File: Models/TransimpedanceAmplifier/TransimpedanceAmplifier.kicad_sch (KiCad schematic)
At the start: 9 parts, among them U1 LM78L15ACMX, U2 LM79L15ACMX, U3 LM78L05ACMX, U4 LM79L05ACMX, U5 LM78L05ACMX, U6 LM79L05ACMX

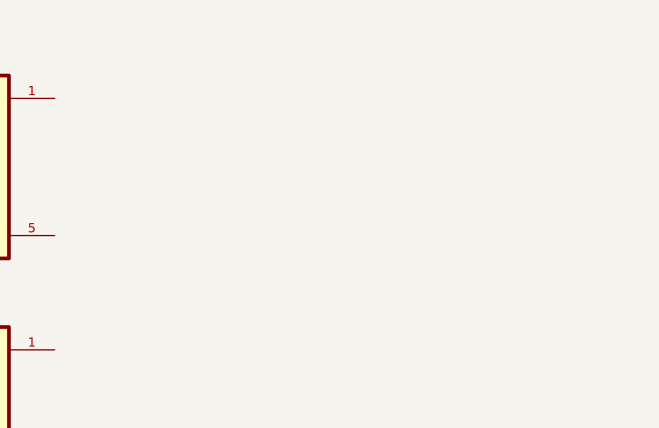
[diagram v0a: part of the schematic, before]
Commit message: Added KiCad libraries for more chips
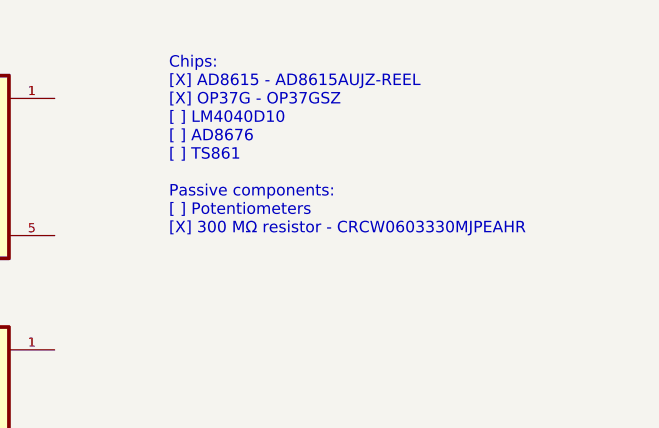
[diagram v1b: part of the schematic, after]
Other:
- note added: "Chips: [X] AD8615 - AD8615AUJZ-REEL [X] OP37G - OP37GSZ [ ] LM4040D10 [ ] AD8676 [ ] TS861 Passive components: [ ] Potentiometers [X] 300 MΩ resistor - CRCW0603330MJPEAHR"
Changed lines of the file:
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@@
 	(generator_version "9.0")
 	(paper "A4")
+	(text "Chips:\n[X] AD8615 - AD8615AUJZ-REEL\n[X] OP37G - OP37GSZ\n[ ] LM4040D10\n[ ] AD8676\n[ ] TS861\n\nPassive components:\n[ ] Potentiometers\n[X] 300 MΩ resistor - CRCW0603330MJPEAHR"
+		(exclude_from_sim no)
+		(at 149.86 38.354 0)
+		(effects
+			(font
+				(size 1.27 1.27)
+			)
+			(justify left)
+		)
+	)
 	(symbol
 		(lib_id "LM78L15ACMX_NOPB:LM78L15ACMX_NOPB")

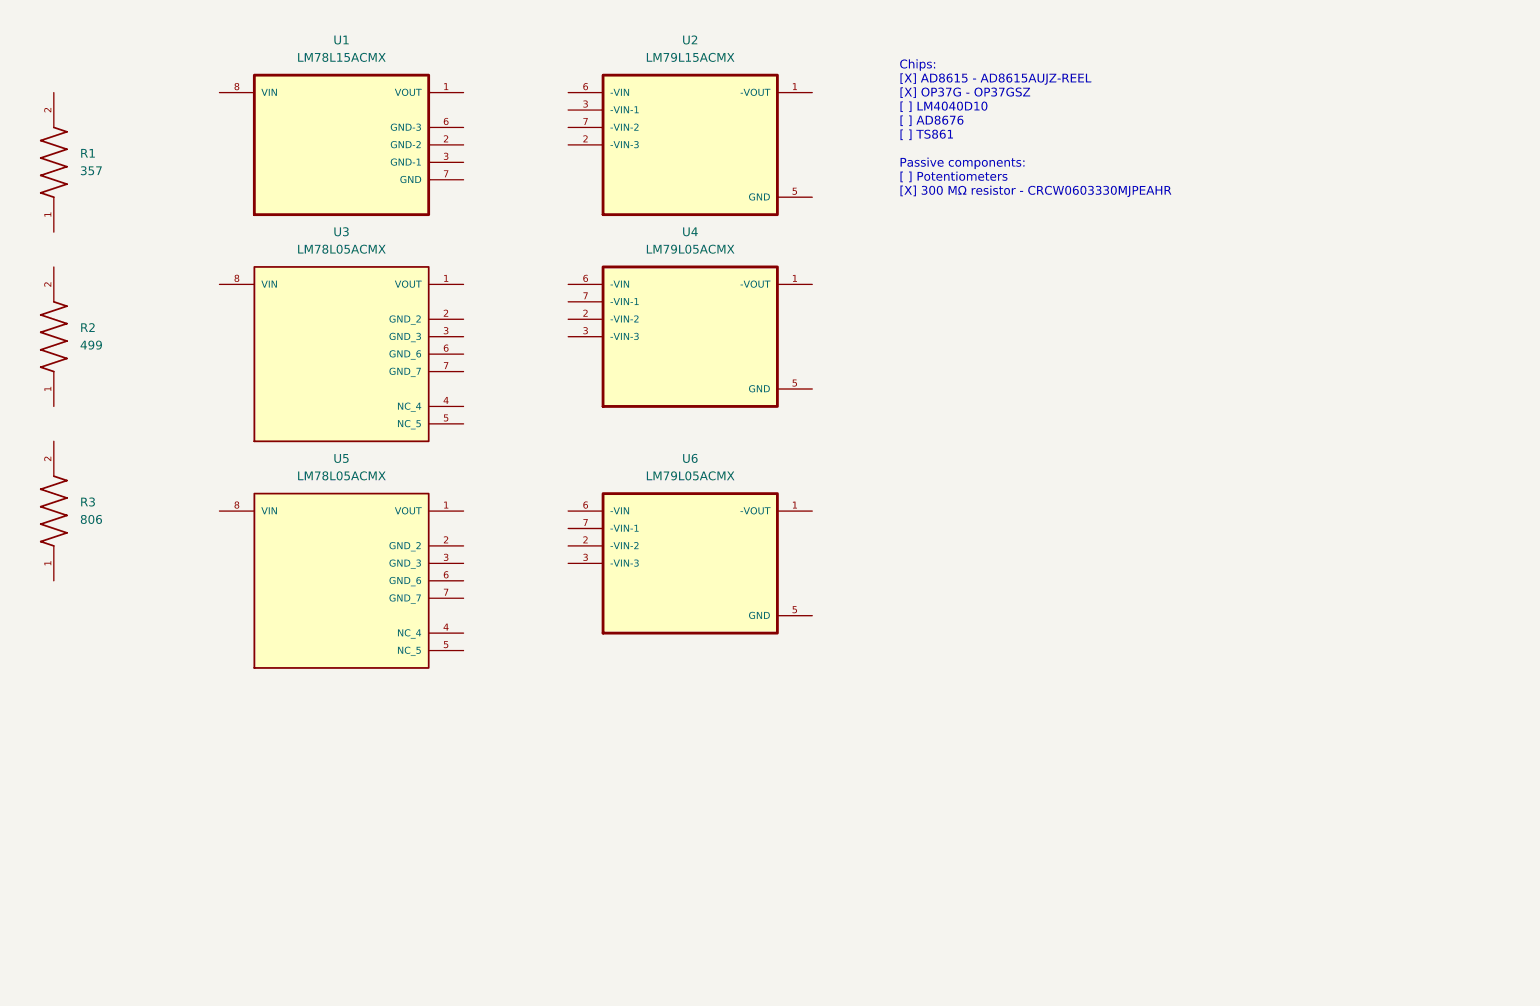
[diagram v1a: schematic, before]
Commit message: Massive cleanup to the libraries for the transimpedance amplifier
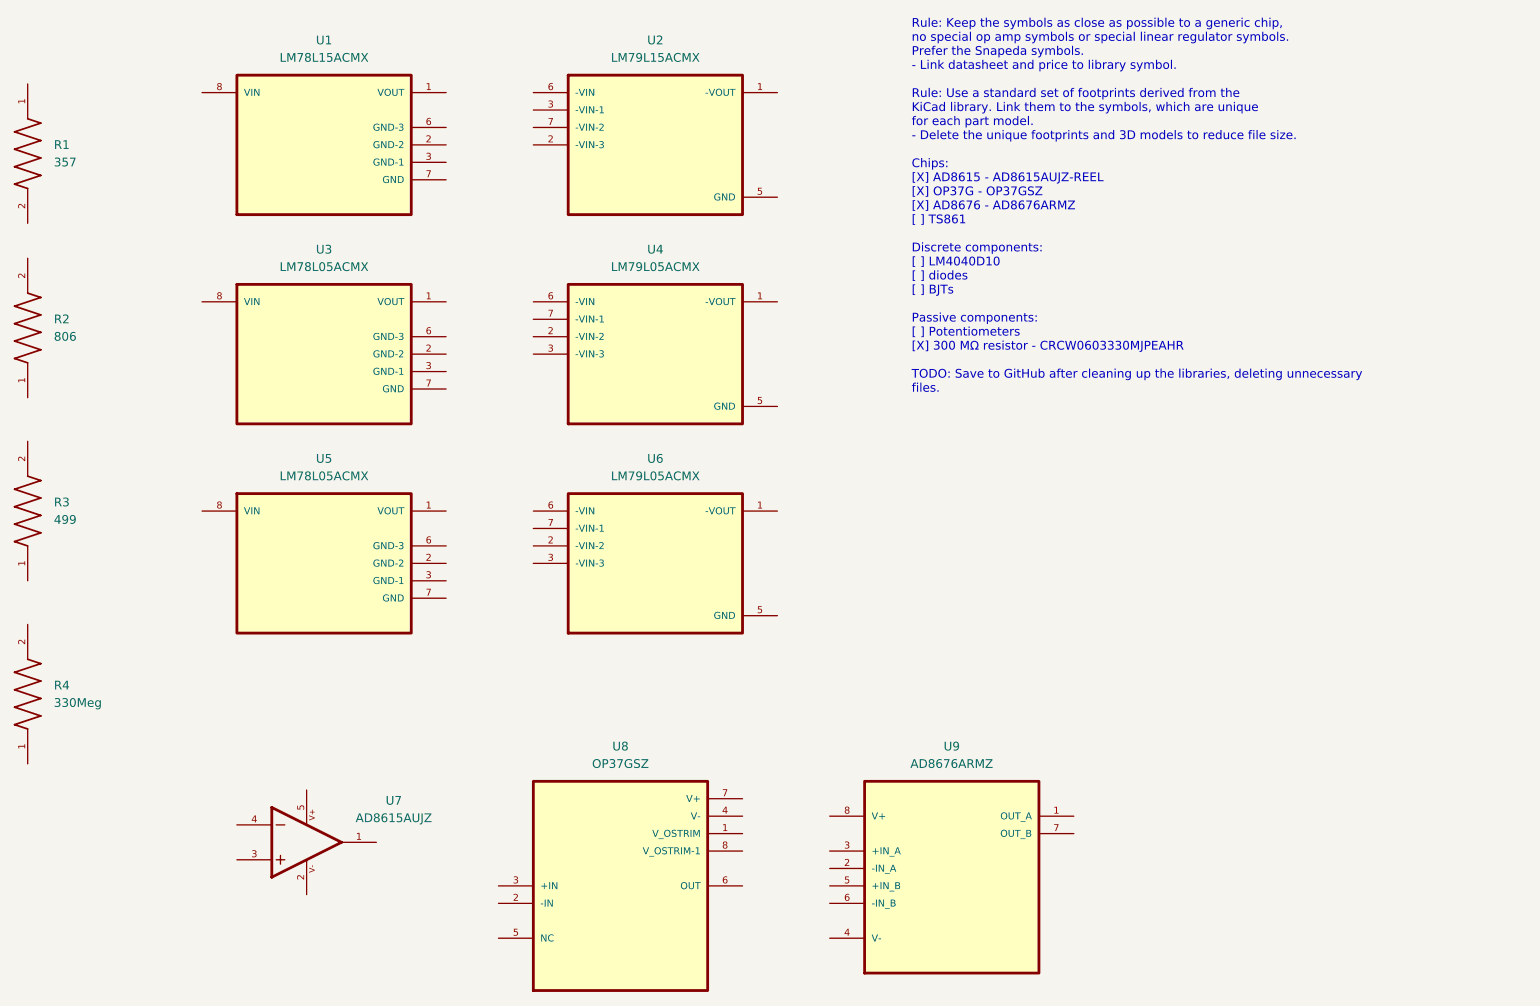
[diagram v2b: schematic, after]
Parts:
- removed R2: 499, CRCW0603499RFKEA:RESC1508X50N, symbol CRCW0603499RFKEA:CRCW0603499RFKEA
- removed R3: 806, CRCW0603806RFKEA:RESC1508X50N, symbol CRCW0603806RFKEA:CRCW0603806RFKEA
- removed U2: LM79L15ACMX, LM79L15ACMX_NOPB_NOPB:SOIC127P599X175-8N, symbol LM79L15ACMX_NOPB_NOPB:LM79L15ACMX_NOPB_NOPB
- added R2: 806, Generic_SMD_Fixed:R_0603_Fixed, symbol CRCW0603806RFKEA:CRCW0603806RFKEA
- added R3: 499, Generic_SMD_Fixed:R_0603_Fixed, symbol CRCW0603499RFKEA:CRCW0603499RFKEA
- added R4: 330Meg, Generic_SMD_Fixed:R_0603_Fixed, symbol CRCW0603330MJPEAHR:CRCW0603330MJPEAHR
- added U2: LM79L15ACMX, Package_SO:SOIC-8_3.9x4.9mm_P1.27mm, symbol LM79L15ACMX_NOPB:LM79L15ACMX_NOPB
- added U7: AD8615AUJZ, Package_TO_SOT_SMD:TSOT-23-5, symbol AD8615AUJZ-REEL:AD8615AUJZ-REEL
- added U8: OP37GSZ, Package_SO:SOIC-8_3.9x4.9mm_P1.27mm, symbol OP37GSZ:OP37GSZ
- added U9: AD8676ARMZ, Package_SO:MSOP-8_3x3mm_P0.65mm, symbol AD8676ARMZ:AD8676ARMZ
- R1: footprint CRCW0603357RFKEA:RESC1508X50N -> Generic_SMD_Fixed:R_0603_Fixed; Availability In Stock -> (none); Check_prices https://www.snapeda.com/parts/CRCW0603357RFKEA/Vishay/view-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 -> (none); Description_1 Resistor;Thick Film;357 Ohms;0.1 W;1%;SMT;0603;TCR 37 ppm/D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 -> (none); MF Vishay -> (none); MP CRCW0603357RFKEA -> (none); Package 1508 Vishay -> (none); SnapEDA_Link https://www.snapeda.com/parts/CRCW0603357RFKEA/Vishay/view-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 -> (none)
- U1: footprint LM78L15ACMX_NOPB:SOIC127P599X175-8N -> Package_SO:SOIC-8_3.9x4.9mm_P1.27mm; Availability In Stock -> (none); Check_prices https://www.snapeda.com/parts/LM78L15ACMX/NOPB/Texas+Instru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 -> (none); Description_1 100-mA, 30-V, linear voltage regulator -> (none); MF Texas Instruments -> (none); MP LM78L15ACMX/NOPB -> (none); Package SOIC-8 Texas Instruments -> (none); SnapEDA_Link https://www.snapeda.com/parts/LM78L15ACMX/NOPB/Texas+Instru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 -> (none)
- U3, U5: footprint LM78L05ACMX_NOPB:SOIC127P599X175-8N -> Package_SO:SOIC-8_3.9x4.9mm_P1.27mm; Availability In Stock -> (none); Check_prices https://www.snapeda.com/parts/LM78L05ACMX/NOPB/Texas+Instru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 -> (none); Description_1 100-mA, 30-V, linear voltage regulator -> (none); MANUFACTURER Texas Instruments -> (none); MAXIMUM_PACKAGE_HEIGHT 1.75mm -> (none); MF Texas Instruments -> (none); MP LM78L05ACMX/NOPB -> (none); PARTREV L -> (none); Package SOIC-8 Texas Instruments -> (none); STANDARD IPC-7351B -> (none); SnapEDA_Link https://www.snapeda.com/parts/LM78L05ACMX/NOPB/Texas+Instru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 -> (none)
- U4, U6: footprint LM79L05ACMX_NOPB:SOIC127P599X175-8N -> Package_SO:SOIC-8_3.9x4.9mm_P1.27mm; Availability In Stock -> (none); Check_prices https://www.snapeda.com/parts/LM79L05ACMX/NOPB/Texas+Instru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 -> (none); Description_1 100-mA, negative linear voltage regulator -> (none); MF Texas Instruments -> (none); MP LM79L05ACMX/NOPB -> (none); Package SOIC-8 Texas Instruments -> (none); SnapEDA_Link https://www.snapeda.com/parts/LM79L05ACMX/NOPB/Texas+Instru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 -> (none)
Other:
- note added: "Rule: Keep the symbols as close as possible to a generic chip, no special op amp symbols or special linear regulator symbols. Prefer the Snapeda symbols. - Link datasheet and price to library symbol. Rule: Use a standard set of footprints derived from the KiCad library. Link them to the symbols, which are unique for each part model. - Delete the unique footprints and 3D models to reduce file size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"
- note removed: "Chips: [X] AD8615 - AD8615AUJZ-REEL [X] OP37G - OP37GSZ [ ] LM4040D10 [ ] AD8676 [ ] TS861 Passive components: [ ] Potentiometers [X] 300 MΩ resistor - CRCW0603330MJPEAHR"
